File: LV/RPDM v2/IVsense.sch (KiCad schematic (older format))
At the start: 3 parts

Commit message: rpdm
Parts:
- U2701: renamed from U?; Full MPN (none) -> ACS71240LLCBTR-050U5
- gave numbers to parts that had none: 2
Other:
- moved on the sheet: C2701, R2701
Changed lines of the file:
@@
 $Descr A4 11693 8268
 encoding utf-8
-Sheet 30 30
+Sheet 27 30
 Title ""
 Date ""
@@
 Text Notes 5350 4200 0    50   ~ 0
 Current sensor
-$Comp
-L Device:R R?
-U 1 1 61C00B2A
-P 4850 3300
-AR Path="/5E546572/61C00B2A" Ref="R?"  Part="1"
-AR Path="/5E545B2D/61C00B2A" Ref="R?"  Part="1"
-AR Path="/5E5461C2/61C00B2A" Ref="R?"  Part="1"
-AR Path="/61BFBFBE/61C00B2A" Ref="R?"  Part="1"
-F 0 "R?" V 4950 3300 50  0000 C CNN
-F 1 "10k" V 4750 3300 50  0000 C CNN
-F 2 "" V 4780 3300 50  0001 C CNN
-F 3 "~" H 4850 3300 50  0001 C CNN
-	1    4850 3300
-	0    1    1    0
-$EndComp
-Text HLabel 4550 3300 0    50   Output ~ 0
-V_Monitor
 NoConn ~ 6100 3800
 Wire Wire Line
@@
 Wire Wire Line
 	5200 3500 5300 3500
-Wire Wire Line
-	6350 3500 6100 3500
-Connection ~ 6350 3500
-Text HLabel 6900 3500 2    50   Input ~ 0
-5V_IN
-Wire Wire Line
-	6900 3500 6350 3500
-Text HLabel 6900 3600 2    50   Output ~ 0
-I_Monitor
-Wire Wire Line
-	6100 3600 6900 3600
-$Comp
-L Device:C C?
-U 1 1 61C00B40
-P 6350 3850
-AR Path="/5E546572/61C00B40" Ref="C?"  Part="1"
-AR Path="/5E545B2D/61C00B40" Ref="C?"  Part="1"
-AR Path="/5E5461C2/61C00B40" Ref="C?"  Part="1"
-AR Path="/61BFBFBE/61C00B40" Ref="C?"  Part="1"
-F 0 "C?" H 6465 3896 50  0000 L CNN
-F 1 "0.1µF" H 6465 3805 50  0000 L CNN
-F 2 "" H 6388 3700 50  0001 C CNN
-F 3 "~" H 6350 3850 50  0001 C CNN
-	1    6350 3850
-	1    0    0    -1
-$EndComp
-Wire Wire Line
-	6350 3700 6350 3500
-Wire Wire Line
-	6350 4000 6350 4100
-$Comp
-L power:GND #PWR?
-U 1 1 61C00B48
-P 6150 4200
-AR Path="/5E546572/61C00B48" Ref="#PWR?"  Part="1"
-AR Path="/5E545B2D/61C00B48" Ref="#PWR?"  Part="1"
-AR Path="/5E5461C2/61C00B48" Ref="#PWR?"  Part="1"
-AR Path="/61BFBFBE/61C00B48" Ref="#PWR?"  Part="1"
-F 0 "#PWR?" H 6150 3950 50  0001 C CNN
-F 1 "GND" H 6155 4027 50  0000 C CNN
-F 2 "" H 6150 4200 50  0001 C CNN
-F 3 "" H 6150 4200 50  0001 C CNN
-	1    6150 4200
-	1    0    0    -1
-$EndComp
-Wire Wire Line
-	6100 3900 6150 3900
-Wire Wire Line
-	6350 4100 6150 4100
-Wire Wire Line
-	6150 4100 6150 4200
-Wire Wire Line
-	6150 3900 6150 4100
-Text Notes 6400 4050 0    50   ~ 0
-Bypass capacitor
 $Comp
 L sensor_current_allegro:ACS71240 U?
@@
 AR Path="/5E5461C2/61C00B54" Ref="U?"  Part="1"
 AR Path="/61C00B54" Ref="U?"  Part="1"
-AR Path="/61BFBFBE/61C00B54" Ref="U?"  Part="1"
-F 0 "U?" H 5700 4050 50  0000 C CNN
+AR Path="/61BFBFBE/61C00B54" Ref="U2701"  Part="1"
+F 0 "U2701" H 5700 4050 50  0000 C CNN
 F 1 "ACS71240" H 5700 3350 50  0000 C CNN
 F 2 "" H 5700 3700 50  0001 C CNN
 F 3 "https://www.allegromicro.com/~/media/Files/Datasheets/ACS71240-Data-Sheet.ashx" H 5700 3700 50  0001 C CNN
+F 4 "ACS71240LLCBTR-050U5" H 5700 3700 50  0001 C CNN "Full MPN"
 	1    5700 3700
 	1    0    0    -1
@@
 Wire Wire Line
 	5300 3900 5200 3900
-Connection ~ 6150 4100
-Wire Wire Line
-	4700 3300 4550 3300
 Text HLabel 4550 3600 0    50   Input ~ 0
 V_IN
@@
 Wire Wire Line
 	5200 3600 5200 3500
-Wire Wire Line
-	5100 3300 5100 3600
 Connection ~ 5100 3600
 Wire Wire Line
 	5100 3600 4550 3600
 Wire Wire Line
-	5100 3300 5000 3300
+	5100 3400 5100 3600
+Wire Wire Line
+	5100 3400 5000 3400
+Text HLabel 4550 3400 0    50   Output ~ 0
+V_Monitor
+Wire Wire Line
+	4700 3400 4550 3400
+Text Notes 6650 3850 0    50   ~ 0
+Bypass capacitor
+$Comp
+L power:GND #PWR?
+U 1 1 61C00B48
+P 6800 3950
+AR Path="/5E546572/61C00B48" Ref="#PWR?"  Part="1"
+AR Path="/5E545B2D/61C00B48" Ref="#PWR?"  Part="1"
+AR Path="/5E5461C2/61C00B48" Ref="#PWR?"  Part="1"
+AR Path="/61BFBFBE/61C00B48" Ref="#PWR02701"  Part="1"
+F 0 "#PWR02701" H 6800 3700 50  0001 C CNN
+F 1 "GND" H 6805 3777 50  0000 C CNN
+F 2 "" H 6800 3950 50  0001 C CNN
+F 3 "" H 6800 3950 50  0001 C CNN
+	1    6800 3950
+	1    0    0    -1
+$EndComp
+Wire Wire Line
+	6800 3900 6800 3950
+Text HLabel 6800 3500 2    50   Input ~ 0
+5V_IN
+Wire Wire Line
+	6100 3900 6600 3900
+Wire Wire Line
+	6600 3850 6600 3900
+Wire Wire Line
+	6600 3550 6600 3500
+$Comp
+L Device:C C?
+U 1 1 61C00B40
+P 6600 3700
+AR Path="/5E546572/61C00B40" Ref="C?"  Part="1"
+AR Path="/5E545B2D/61C00B40" Ref="C?"  Part="1"
+AR Path="/5E5461C2/61C00B40" Ref="C?"  Part="1"
+AR Path="/61BFBFBE/61C00B40" Ref="C2701"  Part="1"
+F 0 "C2701" H 6715 3746 50  0000 L CNN
+F 1 "0.1µF" H 6715 3655 50  0000 L CNN
+F 2 "" H 6638 3550 50  0001 C CNN
+F 3 "~" H 6600 3700 50  0001 C CNN
+	1    6600 3700
+	1    0    0    -1
+$EndComp
+Wire Wire Line
+	6100 3600 6150 3600
+Text HLabel 6150 3600 2    50   Output ~ 0
+I_Monitor
+Connection ~ 6600 3500
+Wire Wire Line
+	6600 3500 6100 3500
+Connection ~ 6600 3900
+Wire Wire Line
+	6600 3500 6800 3500
+Wire Wire Line
+	6600 3900 6800 3900
+$Comp
+L Device:R R?
+U 1 1 61C00B2A
+P 4850 3400
+AR Path="/5E546572/61C00B2A" Ref="R?"  Part="1"
+AR Path="/5E545B2D/61C00B2A" Ref="R?"  Part="1"
+AR Path="/5E5461C2/61C00B2A" Ref="R?"  Part="1"
+AR Path="/61BFBFBE/61C00B2A" Ref="R2701"  Part="1"
+F 0 "R2701" V 4750 3400 50  0000 C CNN
+F 1 "10k" V 4950 3400 50  0000 C CNN
+F 2 "" V 4780 3400 50  0001 C CNN
+F 3 "~" H 4850 3400 50  0001 C CNN
+	1    4850 3400
+	0    1    1    0
+$EndComp
 $EndSCHEMATC

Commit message: rpdm
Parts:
- renumbered C2701 to C7, R2701 to R28, U2701 to U3
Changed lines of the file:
@@
 $Descr A4 11693 8268
 encoding utf-8
-Sheet 27 29
+Sheet 31 32
 Title ""
 Date ""
@@
 AR Path="/5E5461C2/61C00B54" Ref="U?"  Part="1"
 AR Path="/61C00B54" Ref="U?"  Part="1"
-AR Path="/61BFBFBE/61C00B54" Ref="U2701"  Part="1"
-F 0 "U2701" H 5700 4050 50  0000 C CNN
+AR Path="/61BFBFBE/61C00B54" Ref="U3"  Part="1"
+F 0 "U3" H 5700 4050 50  0000 C CNN
 F 1 "ACS71240" H 5700 3350 50  0000 C CNN
 F 2 "" H 5700 3700 50  0001 C CNN
@@
 Wire Wire Line
 	4700 3400 4550 3400
-Text Notes 6650 3850 0    50   ~ 0
-Bypass capacitor
 $Comp
 L power:GND #PWR?
@@
 AR Path="/5E545B2D/61C00B48" Ref="#PWR?"  Part="1"
 AR Path="/5E5461C2/61C00B48" Ref="#PWR?"  Part="1"
-AR Path="/61BFBFBE/61C00B48" Ref="#PWR02701"  Part="1"
-F 0 "#PWR02701" H 6800 3700 50  0001 C CNN
+AR Path="/61BFBFBE/61C00B48" Ref="#PWR038"  Part="1"
+F 0 "#PWR038" H 6800 3700 50  0001 C CNN
 F 1 "GND" H 6805 3777 50  0000 C CNN
 F 2 "" H 6800 3950 50  0001 C CNN
@@
 AR Path="/5E545B2D/61C00B40" Ref="C?"  Part="1"
 AR Path="/5E5461C2/61C00B40" Ref="C?"  Part="1"
-AR Path="/61BFBFBE/61C00B40" Ref="C2701"  Part="1"
-F 0 "C2701" H 6715 3746 50  0000 L CNN
+AR Path="/61BFBFBE/61C00B40" Ref="C7"  Part="1"
+F 0 "C7" H 6715 3746 50  0000 L CNN
 F 1 "0.1µF" H 6715 3655 50  0000 L CNN
 F 2 "" H 6638 3550 50  0001 C CNN
@@
 AR Path="/5E545B2D/61C00B2A" Ref="R?"  Part="1"
 AR Path="/5E5461C2/61C00B2A" Ref="R?"  Part="1"
-AR Path="/61BFBFBE/61C00B2A" Ref="R2701"  Part="1"
-F 0 "R2701" V 4750 3400 50  0000 C CNN
+AR Path="/61BFBFBE/61C00B2A" Ref="R28"  Part="1"
+F 0 "R28" V 4750 3400 50  0000 C CNN
 F 1 "10k" V 4950 3400 50  0000 C CNN
 F 2 "" V 4780 3400 50  0001 C CNN
@@
 	0    1    1    0
 $EndComp
+Text Notes 6650 3850 0    50   ~ 0
+Bypass capacitor
 $EndSCHEMATC

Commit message: rPDM - Started on board layout
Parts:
- C5: renamed from C7; footprint (none) -> Capacitor_SMD:C_0603_1608Metric_Pad1.05x0.95mm_HandSolder
- R2: renamed from R28; footprint (none) -> Resistor_SMD:R_0805_2012Metric_Pad1.15x1.40mm_HandSolder
- U2: renamed from U3; footprint (none) -> eec:Allegro_MicroSystems_LLC-LCB-8-0-0-IPC_A
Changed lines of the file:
@@
 $Descr A4 11693 8268
 encoding utf-8
-Sheet 31 32
+Sheet 4 32
 Title ""
 Date ""
@@
 Wire Wire Line
 	5200 3500 5300 3500
-$Comp
-L sensor_current_allegro:ACS71240 U?
-U 1 1 61C00B54
-P 5700 3700
-AR Path="/5E546572/61C00B54" Ref="U?"  Part="1"
-AR Path="/5E545B2D/61C00B54" Ref="U?"  Part="1"
-AR Path="/5E5461C2/61C00B54" Ref="U?"  Part="1"
-AR Path="/61C00B54" Ref="U?"  Part="1"
-AR Path="/61BFBFBE/61C00B54" Ref="U3"  Part="1"
-F 0 "U3" H 5700 4050 50  0000 C CNN
-F 1 "ACS71240" H 5700 3350 50  0000 C CNN
-F 2 "" H 5700 3700 50  0001 C CNN
-F 3 "https://www.allegromicro.com/~/media/Files/Datasheets/ACS71240-Data-Sheet.ashx" H 5700 3700 50  0001 C CNN
-F 4 "ACS71240LLCBTR-050U5" H 5700 3700 50  0001 C CNN "Full MPN"
-	1    5700 3700
-	1    0    0    -1
-$EndComp
 Wire Wire Line
 	5300 3800 5200 3800
@@
 AR Path="/5E545B2D/61C00B48" Ref="#PWR?"  Part="1"
 AR Path="/5E5461C2/61C00B48" Ref="#PWR?"  Part="1"
-AR Path="/61BFBFBE/61C00B48" Ref="#PWR038"  Part="1"
-F 0 "#PWR038" H 6800 3700 50  0001 C CNN
+AR Path="/61BFBFBE/61C00B48" Ref="#PWR07"  Part="1"
+F 0 "#PWR07" H 6800 3700 50  0001 C CNN
 F 1 "GND" H 6805 3777 50  0000 C CNN
 F 2 "" H 6800 3950 50  0001 C CNN
@@
 AR Path="/5E545B2D/61C00B40" Ref="C?"  Part="1"
 AR Path="/5E5461C2/61C00B40" Ref="C?"  Part="1"
-AR Path="/61BFBFBE/61C00B40" Ref="C7"  Part="1"
-F 0 "C7" H 6715 3746 50  0000 L CNN
+AR Path="/61BFBFBE/61C00B40" Ref="C5"  Part="1"
+F 0 "C5" H 6715 3746 50  0000 L CNN
 F 1 "0.1µF" H 6715 3655 50  0000 L CNN
-F 2 "" H 6638 3550 50  0001 C CNN
+F 2 "Capacitor_SMD:C_0603_1608Metric_Pad1.05x0.95mm_HandSolder" H 6638 3550 50  0001 C CNN
 F 3 "~" H 6600 3700 50  0001 C CNN
 	1    6600 3700
@@
 AR Path="/5E545B2D/61C00B2A" Ref="R?"  Part="1"
 AR Path="/5E5461C2/61C00B2A" Ref="R?"  Part="1"
-AR Path="/61BFBFBE/61C00B2A" Ref="R28"  Part="1"
-F 0 "R28" V 4750 3400 50  0000 C CNN
+AR Path="/61BFBFBE/61C00B2A" Ref="R2"  Part="1"
+F 0 "R2" V 4750 3400 50  0000 C CNN
 F 1 "10k" V 4950 3400 50  0000 C CNN
-F 2 "" V 4780 3400 50  0001 C CNN
+F 2 "Resistor_SMD:R_0805_2012Metric_Pad1.15x1.40mm_HandSolder" V 4780 3400 50  0001 C CNN
 F 3 "~" H 4850 3400 50  0001 C CNN
 	1    4850 3400
@@
 Text Notes 6650 3850 0    50   ~ 0
 Bypass capacitor
+$Comp
+L sensor_current_allegro:ACS71240 U?
+U 1 1 61C00B54
+P 5700 3700
+AR Path="/5E546572/61C00B54" Ref="U?"  Part="1"
+AR Path="/5E545B2D/61C00B54" Ref="U?"  Part="1"
+AR Path="/5E5461C2/61C00B54" Ref="U?"  Part="1"
+AR Path="/61C00B54" Ref="U?"  Part="1"
+AR Path="/61BFBFBE/61C00B54" Ref="U2"  Part="1"
+F 0 "U2" H 5700 4050 50  0000 C CNN
+F 1 "ACS71240" H 5700 3350 50  0000 C CNN
+F 2 "eec:Allegro_MicroSystems_LLC-LCB-8-0-0-IPC_A" H 5700 3700 50  0001 C CNN
+F 3 "https://datasheet.octopart.com/ACS71240LLCBTR-050U5-Allegro-MicroSystems-LLC-datasheet-142380063.pdf" H 5700 3700 50  0001 C CNN
+F 4 "ACS71240LLCBTR-050U5" H 5700 3700 50  0001 C CNN "Full MPN"
+	1    5700 3700
+	1    0    0    -1
+$EndComp
 $EndSCHEMATC

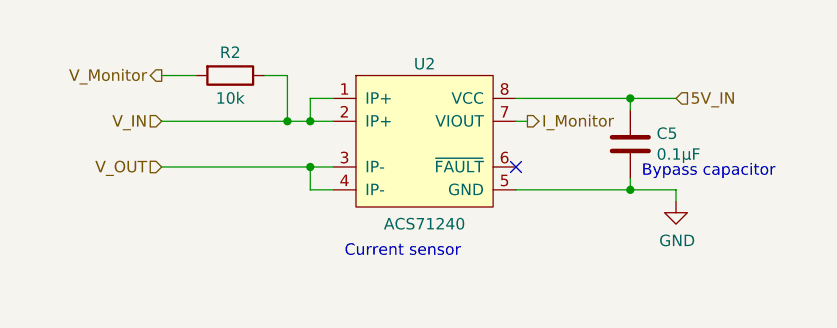
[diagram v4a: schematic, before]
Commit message: rpdm, libraries cleanup
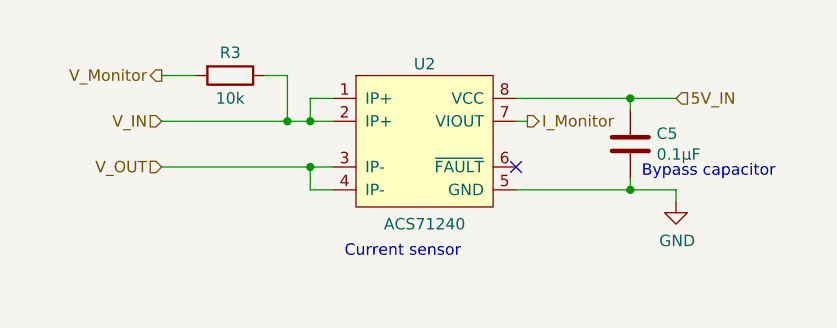
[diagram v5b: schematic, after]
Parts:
- renumbered R2 to R3
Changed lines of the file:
@@
 AR Path="/5E545B2D/61C00B2A" Ref="R?"  Part="1"
 AR Path="/5E5461C2/61C00B2A" Ref="R?"  Part="1"
-AR Path="/61BFBFBE/61C00B2A" Ref="R2"  Part="1"
-F 0 "R2" V 4750 3400 50  0000 C CNN
+AR Path="/61BFBFBE/61C00B2A" Ref="R3"  Part="1"
+F 0 "R3" V 4750 3400 50  0000 C CNN
 F 1 "10k" V 4950 3400 50  0000 C CNN
 F 2 "Resistor_SMD:R_0805_2012Metric_Pad1.15x1.40mm_HandSolder" V 4780 3400 50  0001 C CNN

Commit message: RPDM
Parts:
- U4: renamed from U2; footprint eec:Allegro_MicroSystems_LLC-LCB-8-0-0-IPC_A -> UOWM_Sensors:Allegro_MicroSystems_LLC-LCB-8-0-0-IPC_A
- renumbered C5 to C6, R3 to R36
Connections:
- net I_Monitor renamed 24I_Monitor
- net V_Monitor renamed 24V_Monitor
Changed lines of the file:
@@
 $Descr A4 11693 8268
 encoding utf-8
-Sheet 4 32
+Sheet 30 30
 Title ""
 Date ""
@@
 Text HLabel 4550 3600 0    50   Input ~ 0
 V_IN
-Text HLabel 4550 3800 0    50   Input ~ 0
+Text HLabel 4550 3800 0    50   Output ~ 0
 V_OUT
 Wire Wire Line
@@
 	5100 3400 5000 3400
 Text HLabel 4550 3400 0    50   Output ~ 0
-V_Monitor
+24V_Monitor
 Wire Wire Line
 	4700 3400 4550 3400
@@
 AR Path="/5E545B2D/61C00B48" Ref="#PWR?"  Part="1"
 AR Path="/5E5461C2/61C00B48" Ref="#PWR?"  Part="1"
-AR Path="/61BFBFBE/61C00B48" Ref="#PWR07"  Part="1"
-F 0 "#PWR07" H 6800 3700 50  0001 C CNN
+AR Path="/61BFBFBE/61C00B48" Ref="#PWR043"  Part="1"
+F 0 "#PWR043" H 6800 3700 50  0001 C CNN
 F 1 "GND" H 6805 3777 50  0000 C CNN
 F 2 "" H 6800 3950 50  0001 C CNN
@@
 AR Path="/5E545B2D/61C00B40" Ref="C?"  Part="1"
 AR Path="/5E5461C2/61C00B40" Ref="C?"  Part="1"
-AR Path="/61BFBFBE/61C00B40" Ref="C5"  Part="1"
-F 0 "C5" H 6715 3746 50  0000 L CNN
+AR Path="/61BFBFBE/61C00B40" Ref="C6"  Part="1"
+F 0 "C6" H 6715 3746 50  0000 L CNN
 F 1 "0.1µF" H 6715 3655 50  0000 L CNN
 F 2 "Capacitor_SMD:C_0603_1608Metric_Pad1.05x0.95mm_HandSolder" H 6638 3550 50  0001 C CNN
-F 3 "~" H 6600 3700 50  0001 C CNN
+F 3 "https://api.kemet.com/component-edge/download/datasheet/C0603C104K5RACAUTO7411.pdf" H 6600 3700 50  0001 C CNN
 	1    6600 3700
 	1    0    0    -1
@@
 	6100 3600 6150 3600
 Text HLabel 6150 3600 2    50   Output ~ 0
-I_Monitor
+24I_Monitor
 Connection ~ 6600 3500
 Wire Wire Line
@@
 AR Path="/5E545B2D/61C00B2A" Ref="R?"  Part="1"
 AR Path="/5E5461C2/61C00B2A" Ref="R?"  Part="1"
-AR Path="/61BFBFBE/61C00B2A" Ref="R3"  Part="1"
-F 0 "R3" V 4750 3400 50  0000 C CNN
+AR Path="/61BFBFBE/61C00B2A" Ref="R36"  Part="1"
+F 0 "R36" V 4750 3400 50  0000 C CNN
 F 1 "10k" V 4950 3400 50  0000 C CNN
 F 2 "Resistor_SMD:R_0805_2012Metric_Pad1.15x1.40mm_HandSolder" V 4780 3400 50  0001 C CNN
-F 3 "~" H 4850 3400 50  0001 C CNN
+F 3 "https://www.koaspeer.com/pdfs/RK73H.pdf" H 4850 3400 50  0001 C CNN
 	1    4850 3400
 	0    1    1    0
@@
 AR Path="/5E5461C2/61C00B54" Ref="U?"  Part="1"
 AR Path="/61C00B54" Ref="U?"  Part="1"
-AR Path="/61BFBFBE/61C00B54" Ref="U2"  Part="1"
-F 0 "U2" H 5700 4050 50  0000 C CNN
+AR Path="/61BFBFBE/61C00B54" Ref="U4"  Part="1"
+F 0 "U4" H 5700 4050 50  0000 C CNN
 F 1 "ACS71240" H 5700 3350 50  0000 C CNN
-F 2 "eec:Allegro_MicroSystems_LLC-LCB-8-0-0-IPC_A" H 5700 3700 50  0001 C CNN
+F 2 "UOWM_Sensors:Allegro_MicroSystems_LLC-LCB-8-0-0-IPC_A" H 5700 3700 50  0001 C CNN
 F 3 "https://datasheet.octopart.com/ACS71240LLCBTR-050U5-Allegro-MicroSystems-LLC-datasheet-142380063.pdf" H 5700 3700 50  0001 C CNN
 F 4 "ACS71240LLCBTR-050U5" H 5700 3700 50  0001 C CNN "Full MPN"
